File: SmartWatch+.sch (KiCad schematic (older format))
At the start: 5 parts, among them IC1 DS1315-5+, J1 2-1571586-9, J2 2-1571586-9

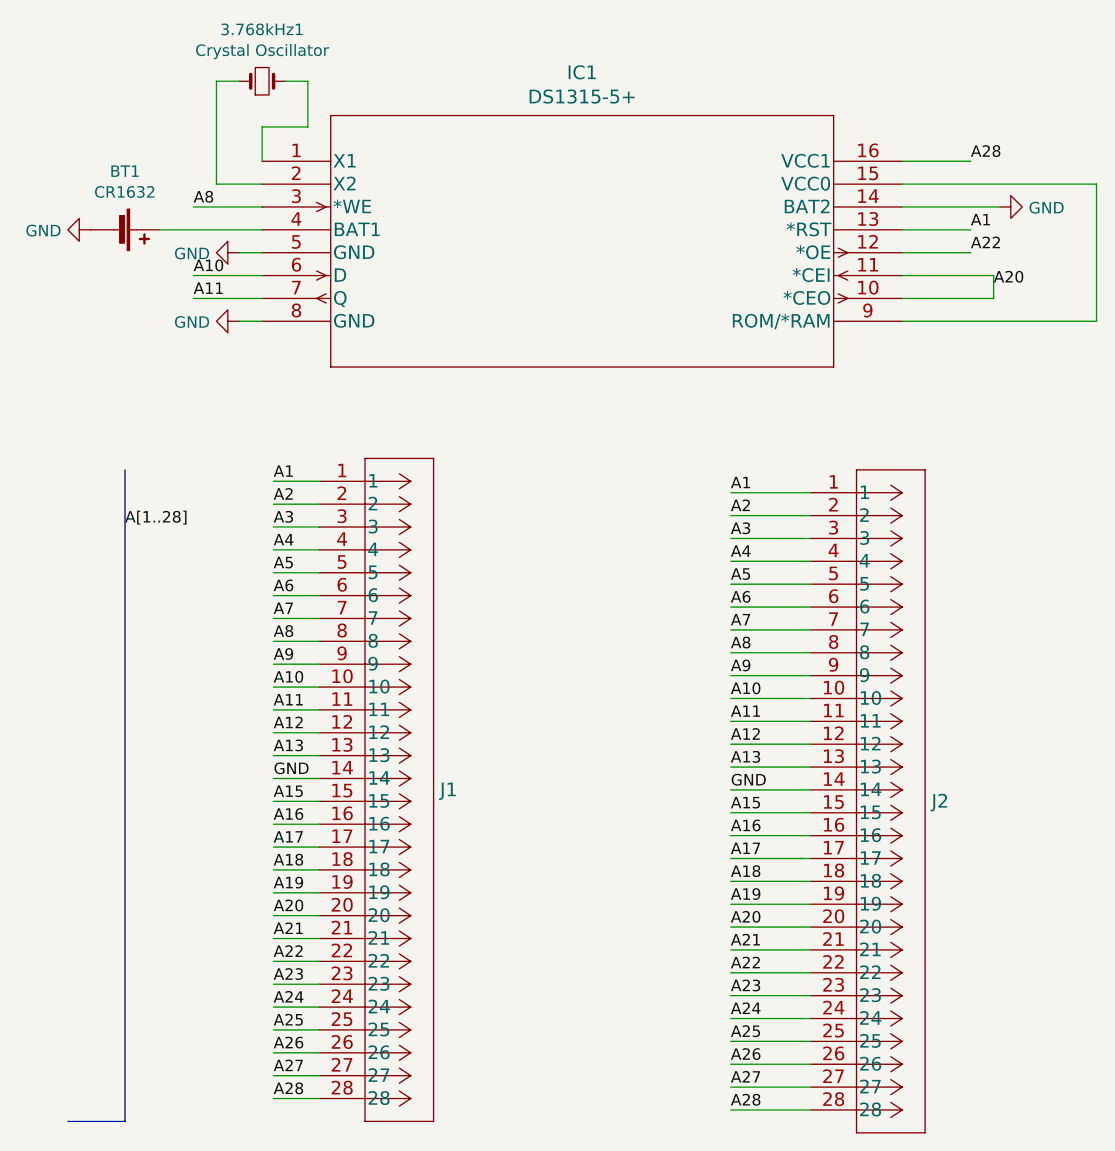
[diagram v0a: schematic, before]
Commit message: Add files via upload
Updated 28-pin Socket to have actual Pin Lables.
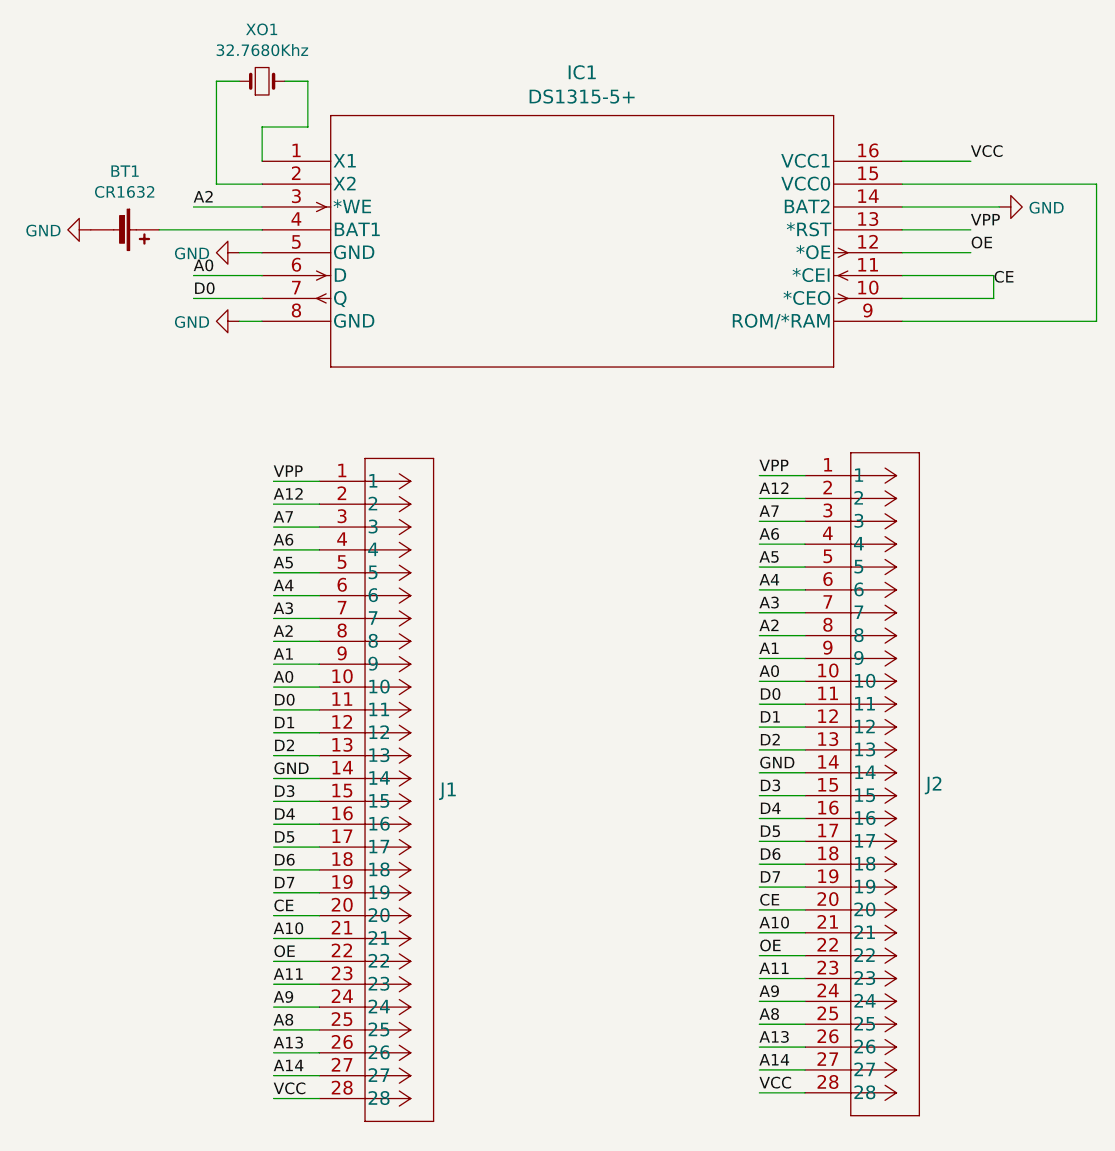
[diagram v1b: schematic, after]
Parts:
- XO1: renamed from 3.768kHz1; value Crystal Oscillator -> 32.7680Khz; footprint Dereks Parts:TC26H -> Dereks_Parts:TC26H
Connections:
- net A21 is gone; now on net A10: J1.21, J2.21
- net A23 is gone; now on net A11: J1.23, J2.23
- net A24 is gone; now on net A9: J1.24, J2.24
- net A25 is gone; now on net A8: J1.25, J2.25
- net A26 is gone; now on net A13: J1.26, J2.26
- net A1: now also J1.9, J2.9; no longer IC1.13 (*RST), J1.1, J2.1
- net A10: no longer IC1.6 (D), J1.10, J2.10
- net A11: no longer IC1.7 (Q), J1.11, J2.11
- net A12: now also J1.2, J2.2; no longer J1.12, J2.12
- net A13: no longer J1.13, J2.13
- net A2: now also IC1.3 (*WE), J1.8, J2.8; no longer J1.2, J2.2
- net A3: now also J1.7, J2.7; no longer J1.3, J2.3
- net A4: now also J1.6, J2.6; no longer J1.4, J2.4
- net A6: now also J1.4, J2.4; no longer J1.6, J2.6
- net A7: now also J1.3, J2.3; no longer J1.7, J2.7
- net A8: no longer IC1.3 (*WE), J1.8, J2.8
- net A9: no longer J1.9, J2.9
- net A15 renamed D3
- net A16 renamed D4
- net A17 renamed D5
- net A18 renamed D6
- net A19 renamed D7
- net A20 renamed CE
- net A22 renamed OE
- net A27 renamed A14
- net A28 renamed VCC
- new net A0: IC1.6 (D), J1.10, J2.10
- new net D0: IC1.7 (Q), J1.11, J2.11
- new net D1: J1.12, J2.12
- new net D2: J1.13, J2.13
- new net VPP: IC1.13 (*RST), J1.1, J2.1
